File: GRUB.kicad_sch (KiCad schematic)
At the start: 61 parts, among them J1 External controller, timer or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, J10 FOOT_SWITCH_JACK, J5 DE15_Receptacle_HighDensity_M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, Q1 2N3904, Q2 2N3904, Q3 2N3904, Q5 2N3904, SW1 R_SWITCH, SW2 U_SWITCH, SW3 B_SWITCH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

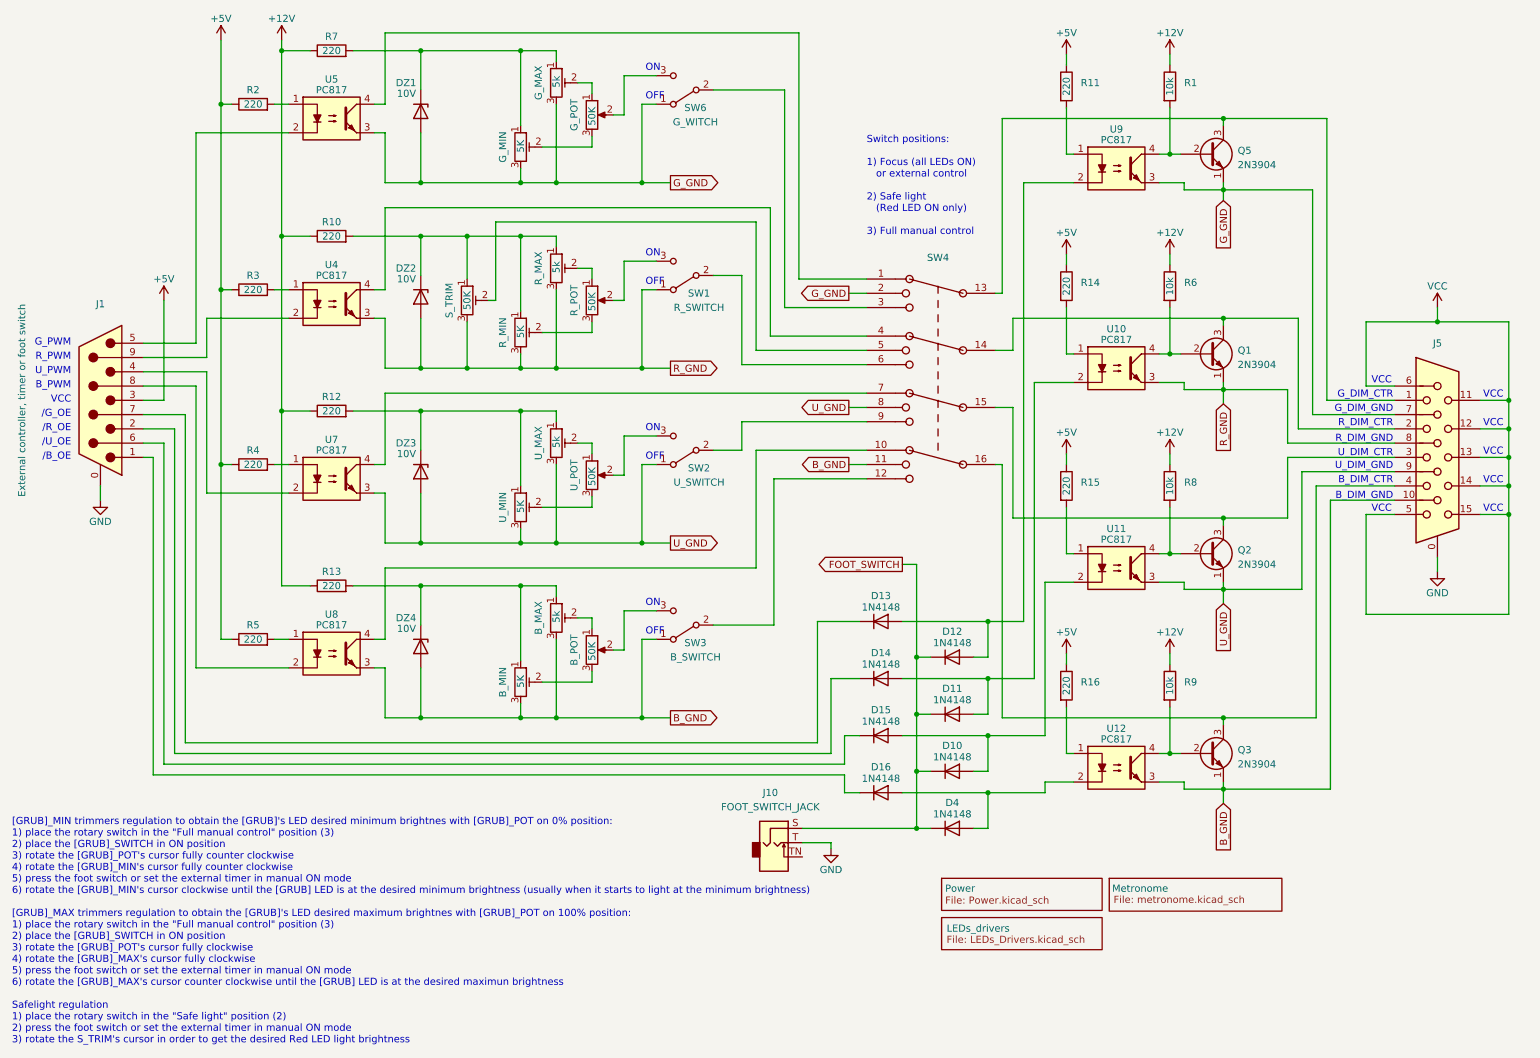
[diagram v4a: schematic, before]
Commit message: Adding capacitors to stabilize voltages, changed the LED driver connector
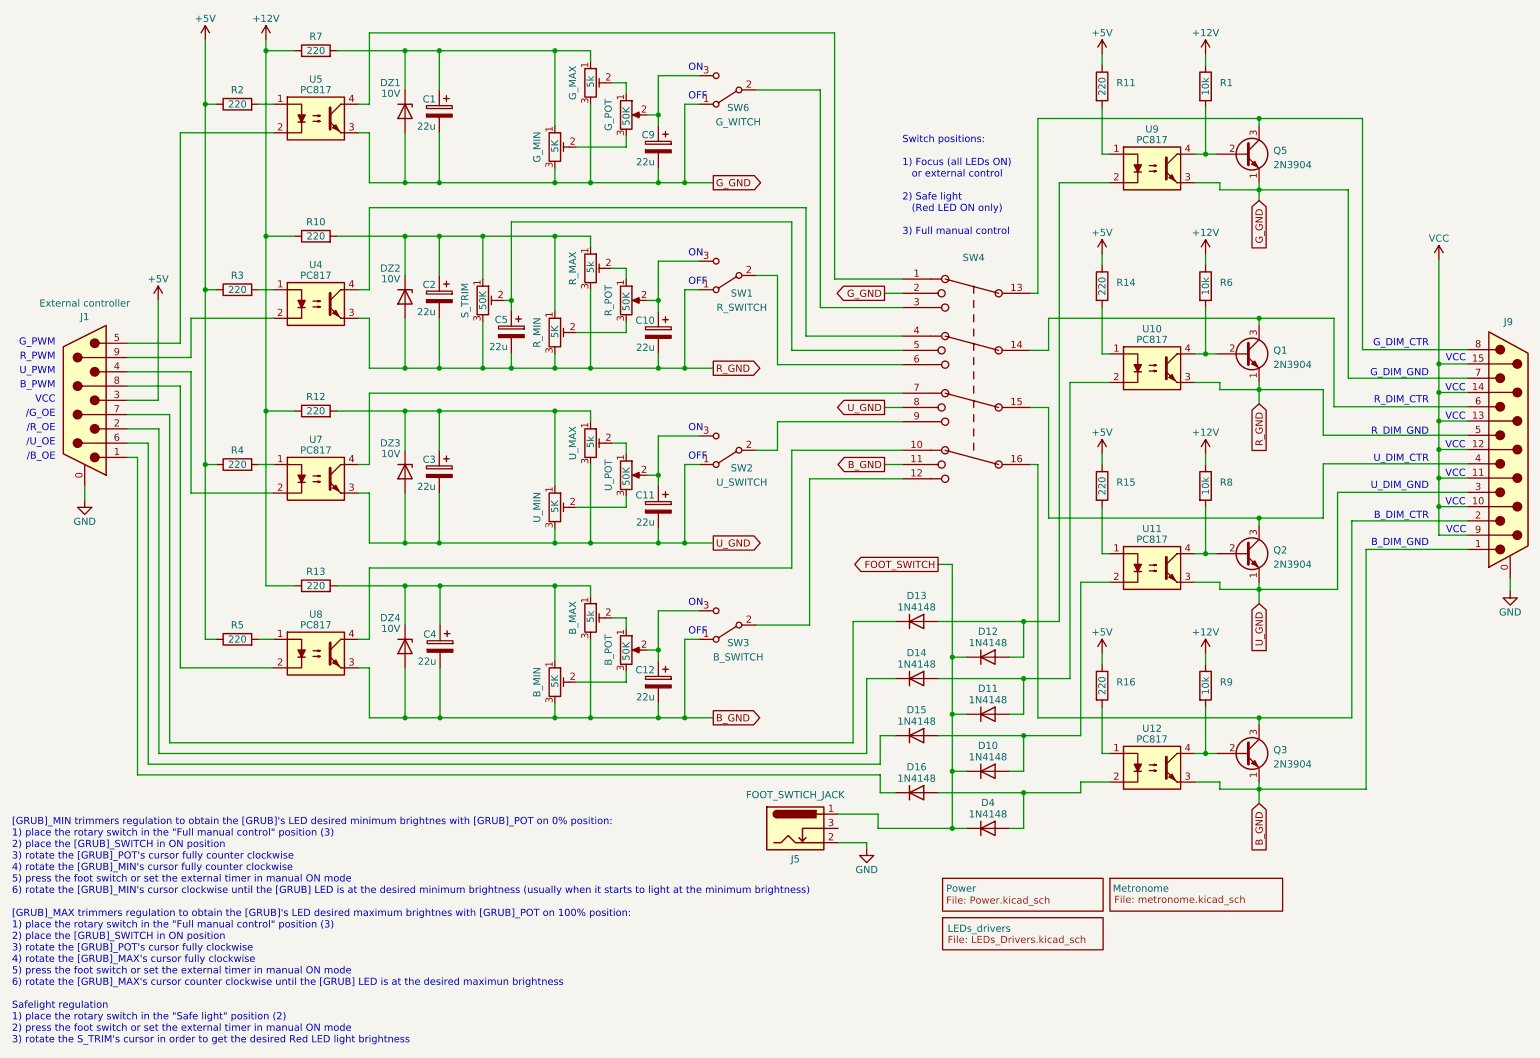
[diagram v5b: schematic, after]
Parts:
- removed J10: FOOT_SWITCH_JACK, symbol Connector_Audio:AudioJack2_SwitchT
- removed J5: DE15_Receptacle_HighDensity_MountingHoles, symbol Connector:DE15_Receptacle_HighDensity_MountingHoles
- added C1, C10, C11, C12, C2, C3, C4, C5, C9: 22u, symbol Device:C_Polarized
- added J5: FOOT_SWTICH_JACK, symbol Connector:Barrel_Jack_Switch
- added J9: DA15_Plug_MountingHoles, symbol Connector:DA15_Plug_MountingHoles
- J1: value External controller, timer or foot switch -> External controller
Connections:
- net B_GND: now also C12.2, C4.2, J9.1
- net FOOT_SWITCH: now also J5.1
- net GND: now also J5.2, J9.0 (PAD)
- net G_GND: now also C1.2, C9.2, J9.7
- net R_GND: now also C10.2, C2.2, C5.2, J9.5
- net U_GND: now also C11.2, C3.2, J9.3
- net VCC: now also J9.10 (P10), J9.11 (P111), J9.12 (P12), J9.13 (P13), J9.14 (P14), J9.15 (P15), J9.9 (P9)
- net at DZ1.1 (K), G_MAX.1, G_MIN.1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: now also C1.1
- net at DZ2.1 (K), R10.2, R_MAX.1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: now also C2.1
- net at R_POT.2, SW1.3 (C): now also C10.1
- net at DZ3.1 (K), R12.2, U_MAX.1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: now also C3.1
- net at G_POT.2, SW6.3 (C): now also C9.1
- net at B_POT.2, SW3.3 (C): now also C12.1
- net at B_MAX.1, B_MIN.1, DZ4.1 (K)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: now also C4.1
- net at Q5.3 (C), SW4.13: now also J9.8
- net at Q1.3 (C), SW4.14: now also J9.6
- net at Q2.3 (C), SW4.15: now also J9.4
- net at Q3.3 (C), SW4.16: now also J9.2
- net at SW4.5, S_TRIM.2: now also C5.1
- net at SW2.3 (C), U_POT.2: now also C11.1
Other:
- moved on the sheet: B_MAX, B_MIN, B_POT, D10, D11, D12, D13, D14, D15, D16, D4, DZ1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

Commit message: - Adding pulldown resistors to keep LEDs drivers OFF when [GRUB]_SWITCHes transits from OFF to ON - Adding op-amps as voltage follower between [GRUB]_POTs and [GRUB]_SWITCHes to guarantee linearity in control voltages
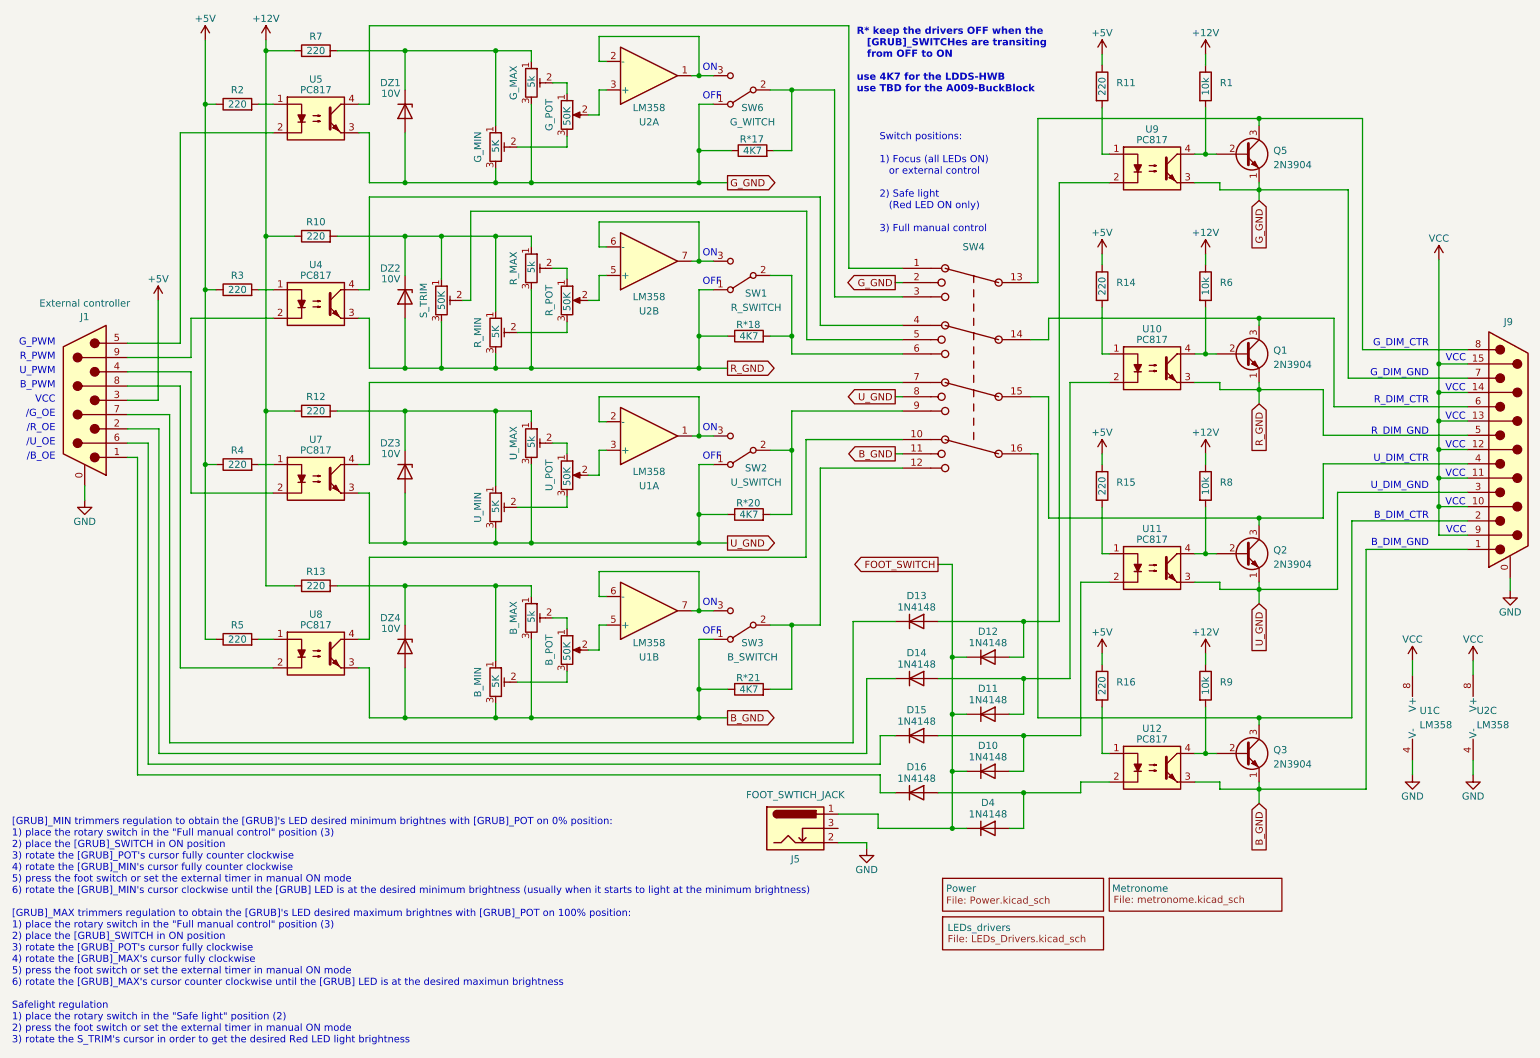
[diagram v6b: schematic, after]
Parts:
- removed C1, C10, C11, C12, C2, C3, C4, C5, C9: 22u, symbol Device:C_Polarized
- added R*17, R*18, R*20, R*21: 4K7, symbol device:R
- added U1, U2: LM358, symbol Amplifier_Operational:LM358
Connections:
- net B_GND: now also R*21.1
- net GND: now also U1.4 (V-), U2.4 (V-)
- net G_GND: now also R*17.1
- net R_GND: now also R*18.1
- net U_GND: now also R*20.1
- net VCC: now also U1.8 (V+), U2.8 (V+)
- net at R_POT.2: now also U2.5 (+); no longer SW1.3 (C)
- net at SW1.2 (B), SW4.6: now also R*18.2
- net at G_POT.2: now also U2.3 (+); no longer SW6.3 (C)
- net at SW3.2 (B), SW4.12: now also R*21.2
- net at SW3.3 (C): now also U1.6 (-), U1.7; no longer B_POT.2
- net at SW4.3, SW6.2 (B): now also R*17.2
- net at SW2.2 (B), SW4.9: now also R*20.2
- net at SW2.3 (C): now also U1.1, U1.2 (-); no longer U_POT.2
- new net: SW1.3 (C), U2.6 (-), U2.7
- new net: U1.3 (+), U_POT.2
- new net: SW6.3 (C), U2.1, U2.2 (-)
- new net: B_POT.2, U1.5 (+)
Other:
- note added: "R* keep the drivers OFF when the [GRUB]_SWITCHes are transiting from OFF to ON use 4K7 for the LDDS-HWB use TBD for the A009-BuckBlock"
- moved on the sheet: B_MAX, B_MIN, B_POT, G_MAX, G_MIN, G_POT, R_MAX, R_MIN, R_POT, SW1, SW2, SW3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
